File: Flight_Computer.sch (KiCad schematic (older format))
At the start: 145 parts, among them IC1 PIC32MZ2048EFH144-I_PL, IC2 FAN4010IL6X_F113, IC3 FAN4010IL6X_F113, J1 ICSP Programming, J2 SC_19-20, J3 UJ2-MBH-1-SMT-TR, J4 47219-2001, Q1 Q_NPN_BEC, Q2 Q_NPN_BEC, U1 STMPS2141STR, U2 STMPS2141STR, U3 BNO055, U4 SN65HVD1050D, U5 SN74LVC1T45DBVR, U6 SN74LVC1T45DBVR, U8 TXB0104PWR

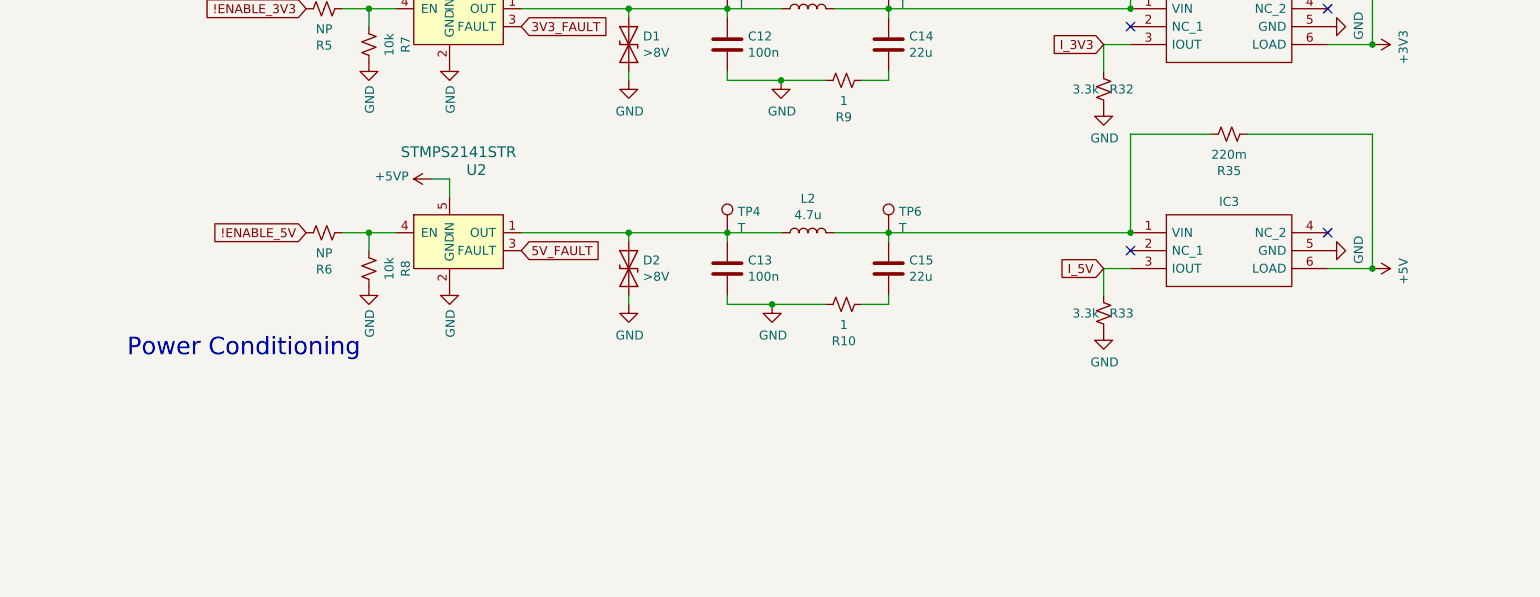
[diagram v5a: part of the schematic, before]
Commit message: Adjusted a few vias to satisfy DRC
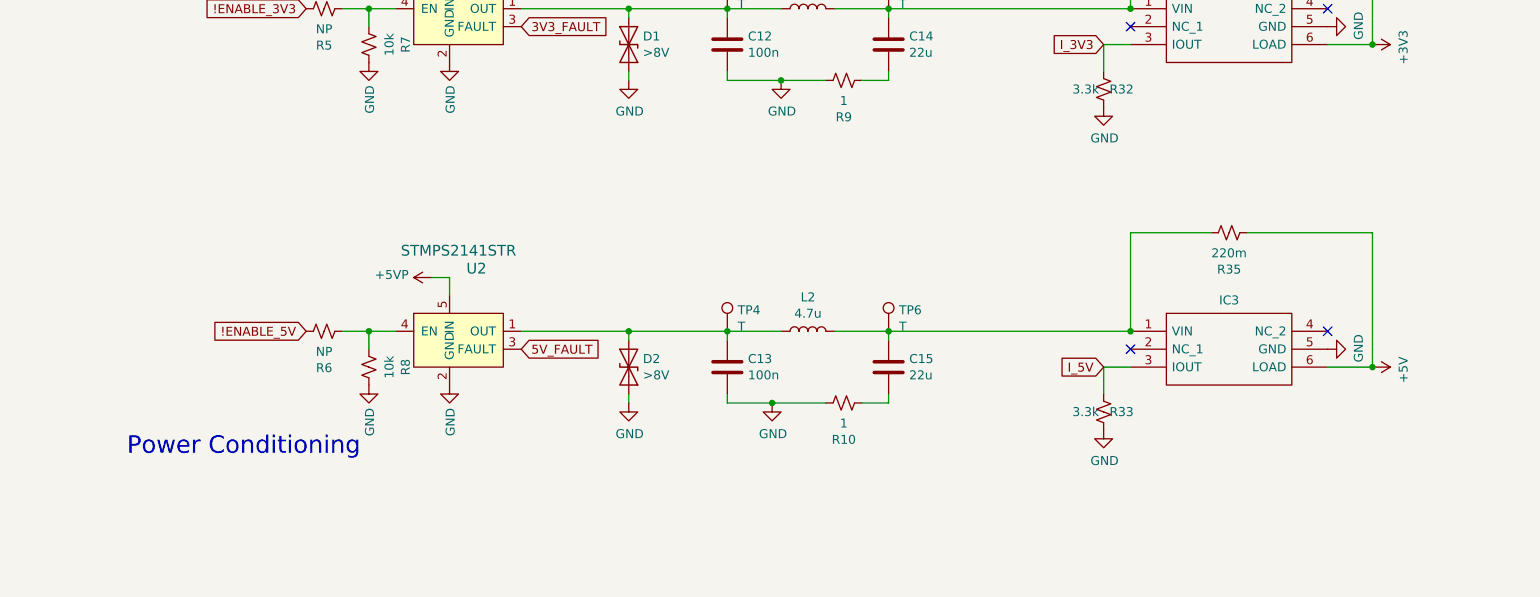
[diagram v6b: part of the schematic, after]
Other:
- moved on the sheet: C13, C15, D2, IC3, L2, R10, R33, R35, R6, R8, TP4, TP6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
